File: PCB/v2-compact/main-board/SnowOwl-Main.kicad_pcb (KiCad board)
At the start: 4 copper layers, 60 x 85 mm, 1 part, among them J1 STACK_2x10

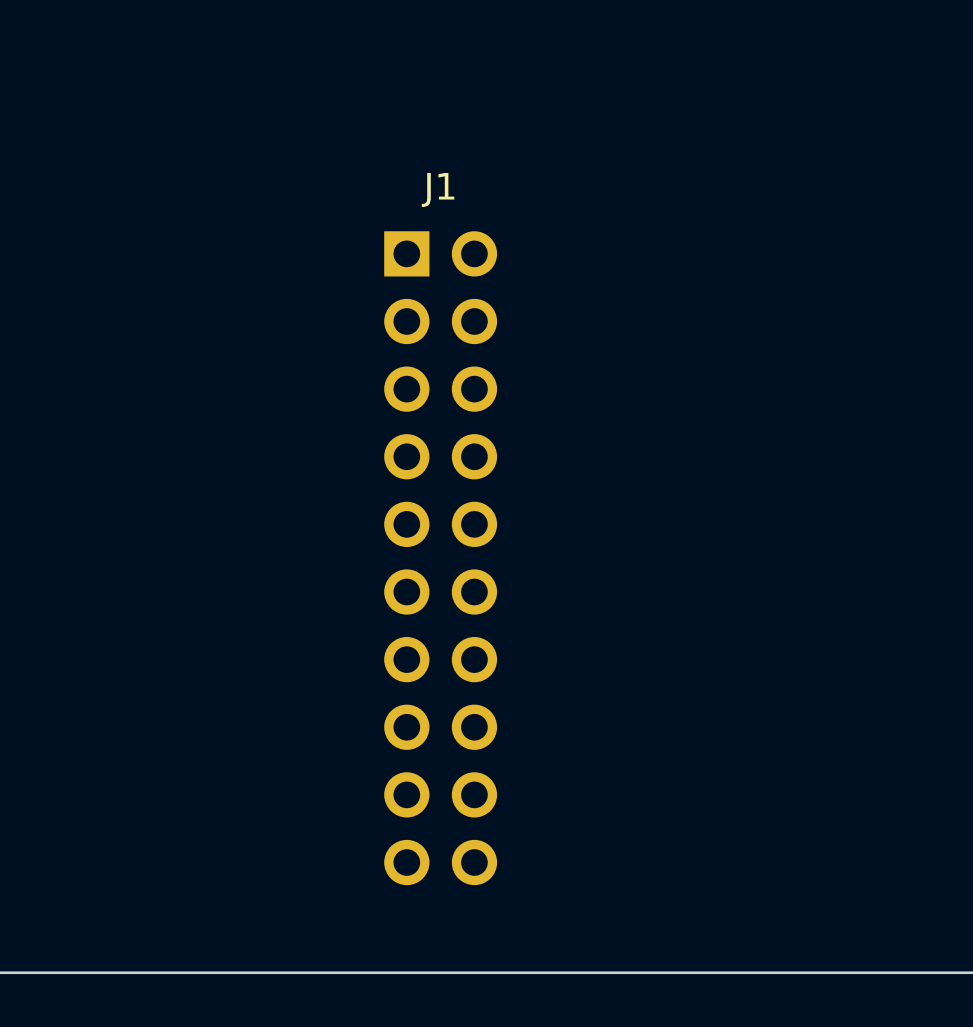
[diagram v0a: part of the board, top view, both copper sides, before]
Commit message: PCB: rework main board to phone-style layout; J1 -> horizontal strip
Main board (per feedback) is now a phone-style split — front is pure UI, back
carries the electronics:
- FRONT: status LEDs at the very top (above the display), TFT rotated to
  LANDSCAPE (sideways), nav buttons below it and moved down. Same feel as the
  ESP32-DIV, sideways screen.
- BACK: ESP32-S3 behind the display, microSD beside it, power + USB-C at the
  bottom-centre edge like a phone.

To keep the centre column free for the landscape display and the bottom-centre
USB-C, J1 is reoriented from a vertical 2x10 to a HORIZONTAL 10x2 strip in the
lower-centre. J1 is the shared mating datum, so the shield's J1 moves to match;
the shield's RV1106 / HTRC110 / bulk-cap zones shift to sit above/below the new
strip (SPI spine still runs north from it). Every v1 capability unchanged.

Updated both .kicad_pcb, both floorplan SVGs, both schematics' zone specs, and
PLACEMENT.md. Verified: files parse, J1 clears all zones, no same-side overlaps.

Co-Authored-By: Claude <noreply@anthropic.com>
Claude-Session: https://claude.ai/code/session_017BEAKBRVwbUCc7Sa2o3Ye7
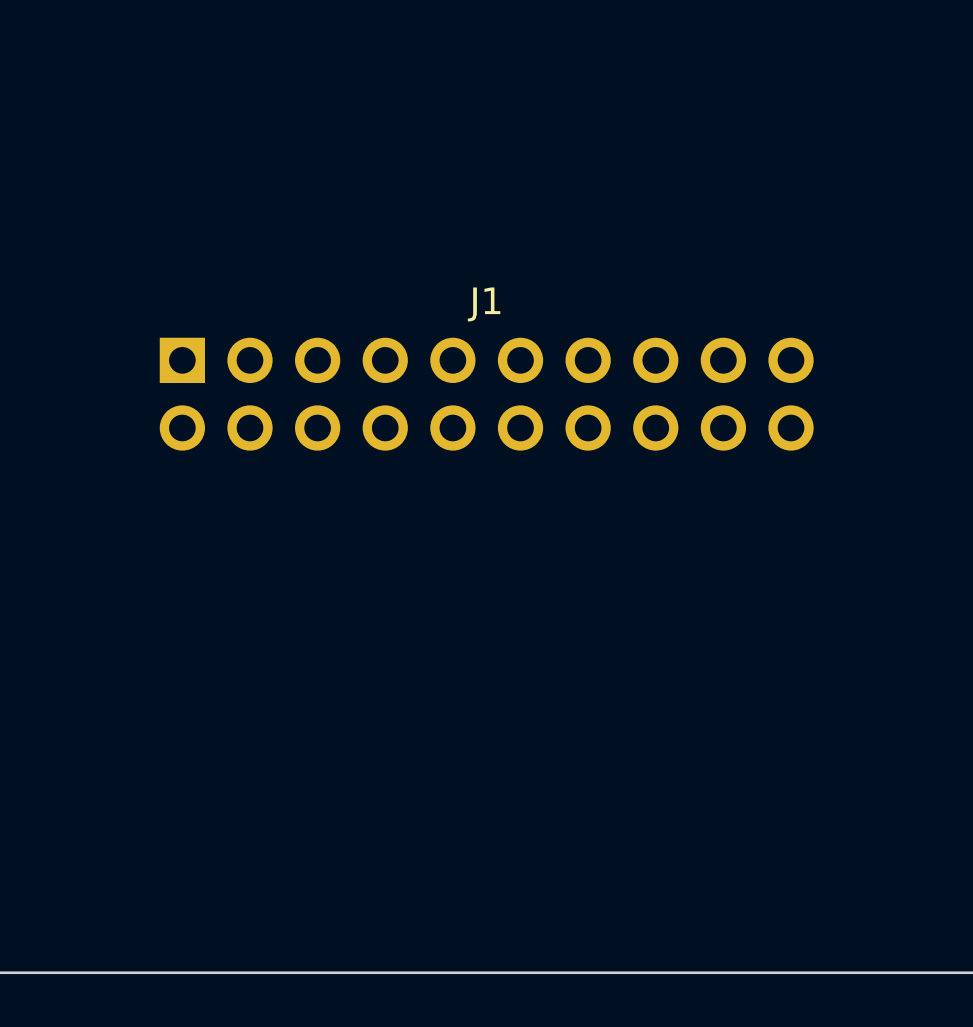
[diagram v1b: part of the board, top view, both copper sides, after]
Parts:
- moved J1 9.33 mm to (48.6, 92.0)
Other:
- board text added: "(BACK) ESP32-S3 (controller/hub)"
- board text added: "(BACK) POWER (LDO / ESD)"
- board text added: "(BACK) USB-C (bottom centre)"
- board text added: "(BACK) microSD (S3)"
- board text added: "NAV BUTTONS (moved down)"
- board text added: "S3 ANT keepout"
- board text added: "STATUS LEDs"
- board text added: "TFT DISPLAY (landscape / sideways)"
- board text added: "USB-C v (back)"
- board text added: "uSD > (back)"
- board text removed: "(BACK) decoupling / GND stitch"
- board text removed: "ESP32-S3 (controller/hub)"
- board text removed: "NAV BUTTONS"
- board text removed: "STATUS LED"
- board text removed: "TFT DISPLAY (SPI)"
- board text removed: "USB-C + POWER (LDO/ESD)"
- board text removed: "USB-C >"
- board text removed: "[S3 ANT keepout]"
- board text removed: "microSD (S3)"
- board text removed: "uSD >"
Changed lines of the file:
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@@
   (gr_text "FRONT zones = User.1   BACK zones = User.2   (floorplan skeleton)" (at 32.0 119.0) (layer "Cmts.User")
     (effects (font (size 1.1 1.1) (thickness 0.18)) (justify left)))
-  (gr_rect (start 34.0 34.0) (end 86.0 58.0) (stroke (width 0.15) (type solid)) (fill none) (layer "User.1"))
-  (gr_text "TFT DISPLAY (SPI)" (at 34.8 36.0) (layer "User.1")
+  (gr_rect (start 49.0 33.0) (end 75.0 39.0) (stroke (width 0.15) (type solid)) (fill none) (layer "User.1"))
+  (gr_text "STATUS LEDs" (at 49.8 35.0) (layer "User.1")
     (effects (font (size 1.1 1.1) (thickness 0.18)) (justify left)))
-  (gr_rect (start 46.0 60.0) (end 74.0 68.0) (stroke (width 0.15) (type solid)) (fill none) (layer "User.1"))
-  (gr_text "NAV BUTTONS" (at 46.8 62.0) (layer "User.1")
+  (gr_rect (start 35.0 41.0) (end 85.0 76.0) (stroke (width 0.15) (type solid)) (fill none) (layer "User.1"))
+  (gr_text "TFT DISPLAY (landscape / sideways)" (at 35.8 43.0) (layer "User.1")
     (effects (font (size 1.1 1.1) (thickness 0.18)) (justify left)))
-  (gr_rect (start 48.0 70.0) (end 72.0 85.0) (stroke (width 0.15) (type solid)) (fill none) (layer "User.1"))
-  (gr_text "ESP32-S3 (controller/hub)" (at 48.8 72.0) (layer "User.1")
+  (gr_rect (start 47.0 80.0) (end 73.0 89.0) (stroke (width 0.15) (type solid)) (fill none) (layer "User.1"))
+  (gr_text "NAV BUTTONS (moved down)" (at 47.8 82.0) (layer "User.1")
     (effects (font (size 1.1 1.1) (thickness 0.18)) (justify left)))
-  (gr_rect (start 33.0 88.0) (end 48.0 112.0) (stroke (width 0.15) (type solid)) (fill none) (layer "User.1"))
-  (gr_text "USB-C + POWER (LDO/ESD)" (at 33.8 90.0) (layer "User.1")
+  (gr_rect (start 44.0 43.0) (end 72.0 70.0) (stroke (width 0.12) (type solid)) (fill none) (layer "User.2"))
+  (gr_text "(BACK) ESP32-S3 (controller/hub)" (at 44.8 45.0) (layer "User.2")
     (effects (font (size 1.1 1.1) (thickness 0.18)) (justify left)))
-  (gr_rect (start 74.0 88.0) (end 87.0 106.0) (stroke (width 0.15) (type solid)) (fill none) (layer "User.1"))
-  (gr_text "microSD (S3)" (at 74.8 90.0) (layer "User.1")
+  (gr_rect (start 74.0 60.0) (end 87.0 80.0) (stroke (width 0.12) (type solid)) (fill none) (layer "User.2"))
+  (gr_text "(BACK) microSD (S3)" (at 74.8 62.0) (layer "User.2")
     (effects (font (size 1.1 1.1) (thickness 0.18)) (justify left)))
-  (gr_rect (start 76.0 60.0) (end 86.0 68.0) (stroke (width 0.15) (type solid)) (fill none) (layer "User.1"))
-  (gr_text "STATUS LED" (at 76.8 62.0) (layer "User.1")
+  (gr_rect (start 34.0 92.0) (end 48.0 112.0) (stroke (width 0.12) (type solid)) (fill none) (layer "User.2"))
+  (gr_text "(BACK) POWER (LDO / ESD)" (at 34.8 94.0) (layer "User.2")
     (effects (font (size 1.1 1.1) (thickness 0.18)) (justify left)))
-  (gr_rect (start 50.0 70.0) (end 70.0 85.0) (stroke (width 0.12) (type solid)) (fill none) (layer "User.2"))
-  (gr_text "(BACK) decoupling / GND stitch" (at 50.8 72.0) (layer "User.2")
+  (gr_rect (start 53.0 107.0) (end 69.0 114.0) (stroke (width 0.12) (type solid)) (fill none) (layer "User.2"))
+  (gr_text "(BACK) USB-C (bottom centre)" (at 53.8 109.0) (layer "User.2")
     (effects (font (size 1.1 1.1) (thickness 0.18)) (justify left)))
-  (gr_text "USB-C >" (at 31.5 100.0) (layer "Cmts.User")
+  (gr_text "S3 ANT keepout" (at 33.5 41.5) (layer "Cmts.User")
     (effects (font (size 1.0 1.0) (thickness 0.15)) (justify left)))
-  (gr_text "uSD >" (at 87.5 97.0) (layer "Cmts.User")
+  (gr_text "USB-C v (back)" (at 54.0 113.5) (layer "Cmts.User")
     (effects (font (size 1.0 1.0) (thickness 0.15)) (justify left)))
-  (gr_text "[S3 ANT keepout]" (at 36.0 71.0) (layer "Cmts.User")
+  (gr_text "uSD > (back)" (at 87.5 70.0) (layer "Cmts.User")
     (effects (font (size 1.0 1.0) (thickness 0.15)) (justify left)))
   (footprint "SnowOwl:StackHeader_2x10" (layer "F.Cu")
-    (at 57.0 88.0)
+    (at 48.57 92.0)
     (descr "SnowOwl 2x10 2.54mm inter-board stack header (shared datum)")
     (attr through_hole)
-    (fp_text reference "J1" (at 1.27 -2.5) (layer "F.SilkS")
+    (fp_text reference "J1" (at 11.43 -2.2) (layer "F.SilkS")
       (effects (font (size 1 1) (thickness 0.15))))
-    (fp_text value "STACK_2x10" (at 1.27 25.4) (layer "F.Fab")
+    (fp_text value "STACK_2x10" (at 11.43 4.7) (layer "F.Fab")
       (effects (font (size 1 1) (thickness 0.15))))
     (pad "1" thru_hole rect (at 0.0 0.0) (size 1.7 1.7) (drill 1.0) (layers "*.Cu" "*.Mask"))
     (pad "2" thru_hole oval (at 2.54 0.0) (size 1.7 1.7) (drill 1.0) (layers "*.Cu" "*.Mask"))
-    (pad "3" thru_hole oval (at 0.0 2.54) (size 1.7 1.7) (drill 1.0) (layers "*.Cu" "*.Mask"))
-    (pad "4" thru_hole oval (at 2.54 2.54) (size 1.7 1.7) (drill 1.0) (layers "*.Cu" "*.Mask"))
-    (pad "5" thru_hole oval (at 0.0 5.08) (size 1.7 1.7) (drill 1.0) (layers "*.Cu" "*.Mask"))
-    (pad "6" thru_hole oval (at 2.54 5.08) (size 1.7 1.7) (drill 1.0) (layers "*.Cu" "*.Mask"))
-    (pad "7" thru_hole oval (at 0.0 7.62) (size 1.7 1.7) (drill 1.0) (layers "*.Cu" "*.Mask"))
-    (pad "8" thru_hole oval (at 2.54 7.62) (size 1.7 1.7) (drill 1.0) (layers "*.Cu" "*.Mask"))
-    (pad "9" thru_hole oval (at 0.0 10.16) (size 1.7 1.7) (drill 1.0) (layers "*.Cu" "*.Mask"))
-    (pad "10" thru_hole oval (at 2.54 10.16) (size 1.7 1.7) (drill 1.0) (layers "*.Cu" "*.Mask"))
-    (pad "11" thru_hole oval (at 0.0 12.7) (size 1.7 1.7) (drill 1.0) (layers "*.Cu" "*.Mask"))
-    (pad "12" thru_hole oval (at 2.54 12.7) (size 1.7 1.7) (drill 1.0) (layers "*.Cu" "*.Mask"))
-    (pad "13" thru_hole oval (at 0.0 15.24) (size 1.7 1.7) (drill 1.0) (layers "*.Cu" "*.Mask"))
-    (pad "14" thru_hole oval (at 2.54 15.24) (size 1.7 1.7) (drill 1.0) (layers "*.Cu" "*.Mask"))
-    (pad "15" thru_hole oval (at 0.0 17.78) (size 1.7 1.7) (drill 1.0) (layers "*.Cu" "*.Mask"))
-    (pad "16" thru_hole oval (at 2.54 17.78) (size 1.7 1.7) (drill 1.0) (layers "*.Cu" "*.Mask"))
-    (pad "17" thru_hole oval (at 0.0 20.32) (size 1.7 1.7) (drill 1.0) (layers "*.Cu" "*.Mask"))
-    (pad "18" thru_hole oval (at 2.54 20.32) (size 1.7 1.7) (drill 1.0) (layers "*.Cu" "*.Mask"))
-    (pad "19" thru_hole oval (at 0.0 22.86) (size 1.7 1.7) (drill 1.0) (layers "*.Cu" "*.Mask"))
-    (pad "20" thru_hole oval (at 2.54 22.86) (size 1.7 1.7) (drill 1.0) (layers "*.Cu" "*.Mask"))
+    (pad "3" thru_hole oval (at 5.08 0.0) (size 1.7 1.7) (drill 1.0) (layers "*.Cu" "*.Mask"))
+    (pad "4" thru_hole oval (at 7.62 0.0) (size 1.7 1.7) (drill 1.0) (layers "*.Cu" "*.Mask"))
+    (pad "5" thru_hole oval (at 10.16 0.0) (size 1.7 1.7) (drill 1.0) (layers "*.Cu" "*.Mask"))
+    (pad "6" thru_hole oval (at 12.7 0.0) (size 1.7 1.7) (drill 1.0) (layers "*.Cu" "*.Mask"))
+    (pad "7" thru_hole oval (at 15.24 0.0) (size 1.7 1.7) (drill 1.0) (layers "*.Cu" "*.Mask"))
+    (pad "8" thru_hole oval (at 17.78 0.0) (size 1.7 1.7) (drill 1.0) (layers "*.Cu" "*.Mask"))
+    (pad "9" thru_hole oval (at 20.32 0.0) (size 1.7 1.7) (drill 1.0) (layers "*.Cu" "*.Mask"))
+    (pad "10" thru_hole oval (at 22.86 0.0) (size 1.7 1.7) (drill 1.0) (layers "*.Cu" "*.Mask"))
+    (pad "11" thru_hole oval (at 0.0 2.54) (size 1.7 1.7) (drill 1.0) (layers "*.Cu" "*.Mask"))
+    (pad "12" thru_hole oval (at 2.54 2.54) (size 1.7 1.7) (drill 1.0) (layers "*.Cu" "*.Mask"))
+    (pad "13" thru_hole oval (at 5.08 2.54) (size 1.7 1.7) (drill 1.0) (layers "*.Cu" "*.Mask"))
+    (pad "14" thru_hole oval (at 7.62 2.54) (size 1.7 1.7) (drill 1.0) (layers "*.Cu" "*.Mask"))
+    (pad "15" thru_hole oval (at 10.16 2.54) (size 1.7 1.7) (drill 1.0) (layers "*.Cu" "*.Mask"))
+    (pad "16" thru_hole oval (at 12.7 2.54) (size 1.7 1.7) (drill 1.0) (layers "*.Cu" "*.Mask"))
+    (pad "17" thru_hole oval (at 15.24 2.54) (size 1.7 1.7) (drill 1.0) (layers "*.Cu" "*.Mask"))
+    (pad "18" thru_hole oval (at 17.78 2.54) (size 1.7 1.7) (drill 1.0) (layers "*.Cu" "*.Mask"))
+    (pad "19" thru_hole oval (at 20.32 2.54) (size 1.7 1.7) (drill 1.0) (layers "*.Cu" "*.Mask"))
+    (pad "20" thru_hole oval (at 22.86 2.54) (size 1.7 1.7) (drill 1.0) (layers "*.Cu" "*.Mask"))
   )
-  (gr_text "J1 STACK (datum: shared X/Y on both boards)" (at 55.0 112.5) (layer "Cmts.User")
+  (gr_text "J1 STACK (datum: shared X/Y on both boards)" (at 48.57 97.0) (layer "Cmts.User")
     (effects (font (size 1.0 1.0) (thickness 0.15)) (justify left)))
 )
